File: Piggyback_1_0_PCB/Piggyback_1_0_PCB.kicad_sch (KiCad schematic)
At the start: 39 parts, among them J1 Conn_01x04_Female, J10 Conn_02x04_Odd_Even, J11 Conn_02x04_Odd_Even, J12 Conn_01x04_Female, J13 Conn_01x04_Female, J2 Conn_02x04_Odd_Even, J3 Conn_01x04_Female, J4 Conn_02x04_Odd_Even, J5 Conn_01x04_Female, J6 Conn_01x04_Female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

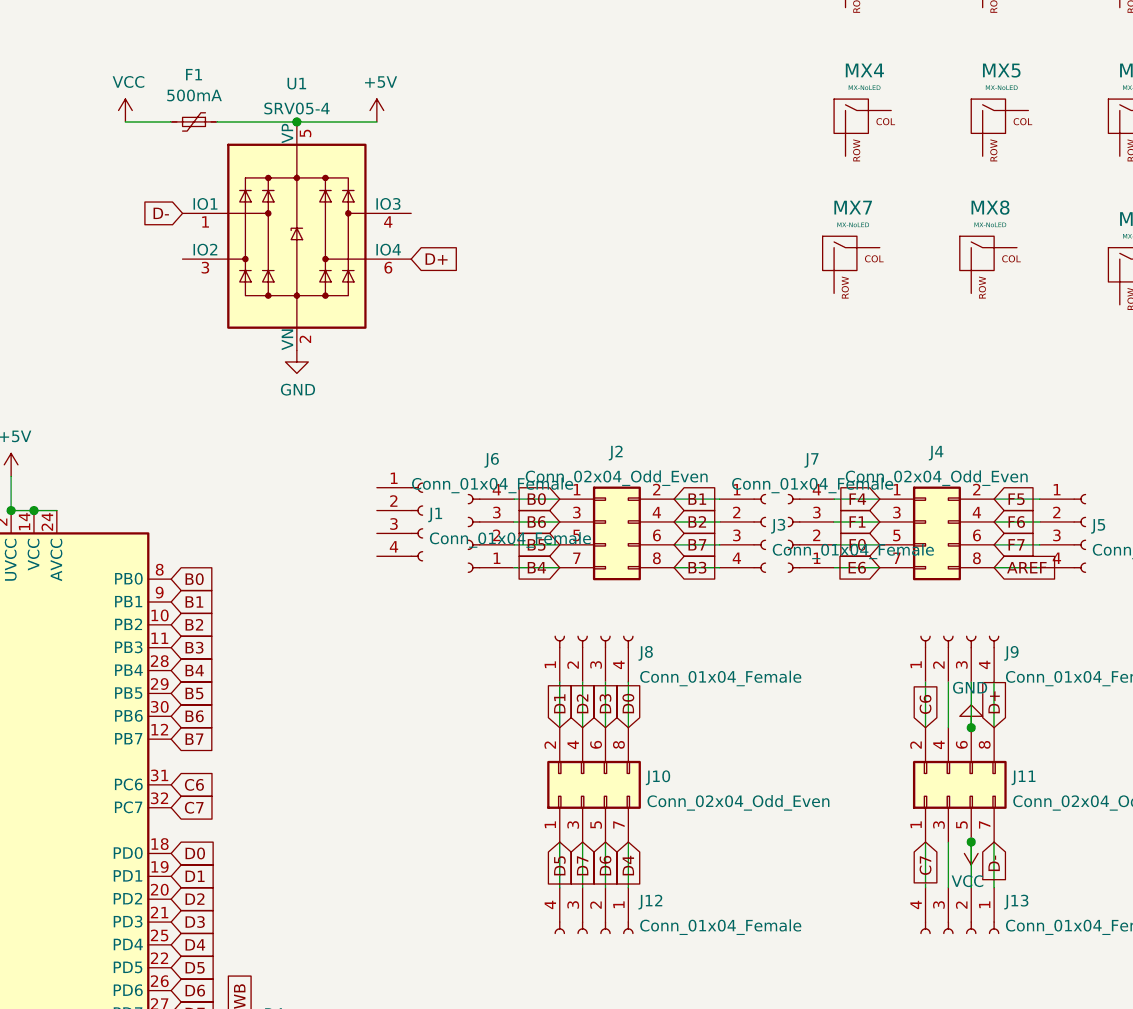
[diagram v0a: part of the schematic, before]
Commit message: Connected NC pads to GND and 5V
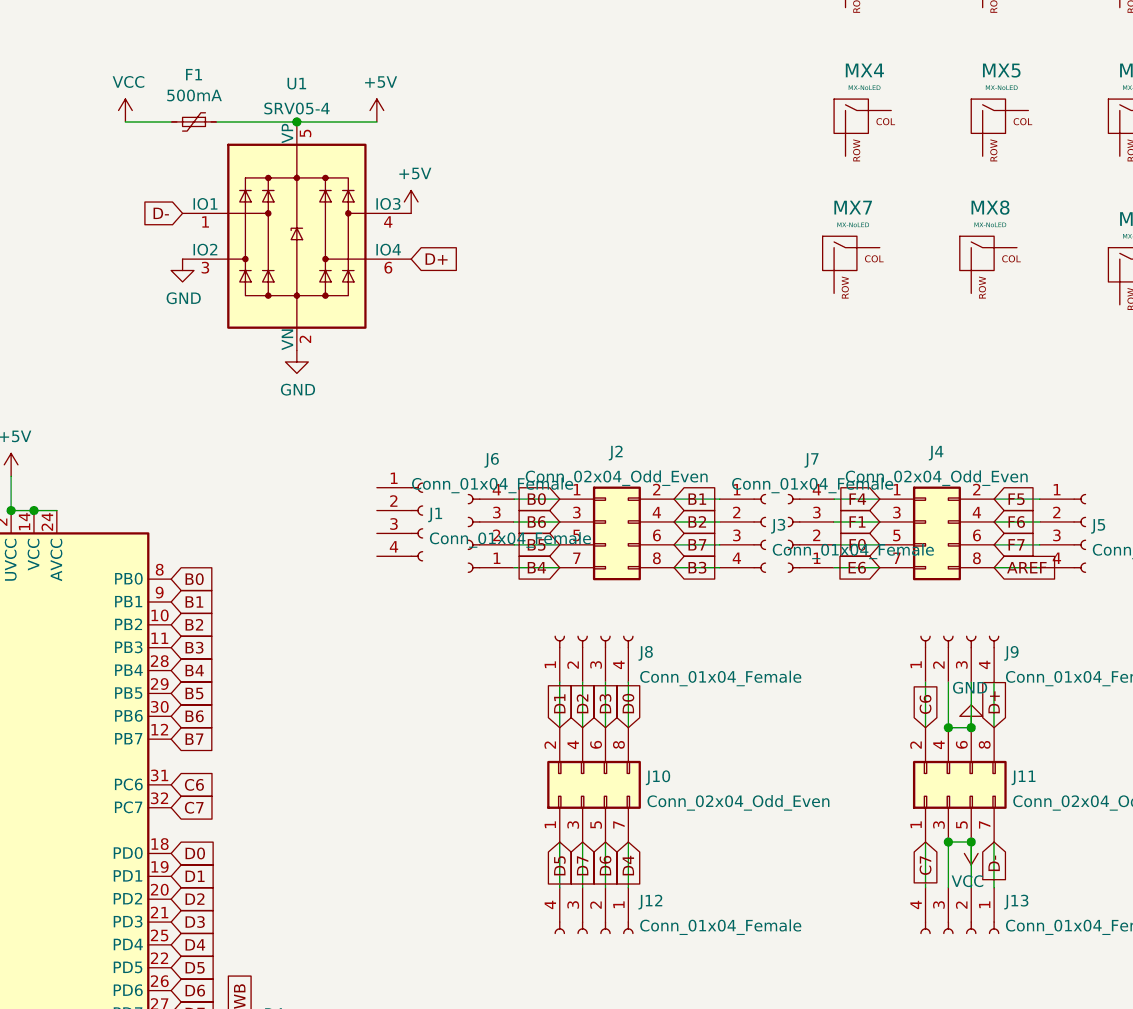
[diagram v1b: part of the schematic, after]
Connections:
- net +5V: now also U1.4 (IO3)
- net GND: now also J11.4 (Pin_4), J9.2 (Pin_2), U1.3 (IO2)
- net VCC: now also J11.3 (Pin_3), J13.3 (Pin_3)
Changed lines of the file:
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@@
   (junction (at 58.42 97.79) (diameter 1.016) (color 0 0 0 0))
   (junction (at 87.63 54.61) (diameter 1.016) (color 0 0 0 0))
+  (junction (at 160.02 121.92) (diameter 1.016) (color 0 0 0 0))
+  (junction (at 160.02 134.62) (diameter 1.016) (color 0 0 0 0))
   (junction (at 162.56 121.92) (diameter 1.016) (color 0 0 0 0))
   (junction (at 162.56 134.62) (diameter 1.016) (color 0 0 0 0))
@@
     (stroke (width 0) (type solid) (color 0 0 0 0))
   )
+  (wire (pts (xy 160.02 121.92) (xy 162.56 121.92))
+    (stroke (width 0) (type solid) (color 0 0 0 0))
+  )
+  (wire (pts (xy 160.02 134.62) (xy 162.56 134.62))
+    (stroke (width 0) (type solid) (color 0 0 0 0))
+  )
   (wire (pts (xy 160.02 139.7) (xy 160.02 134.62))
     (stroke (width 0) (type solid) (color 0 0 0 0))
@@
     (pin "1")
   )
+  (symbol (lib_id "power:+5V") (at 100.33 64.77 0) (unit 1)
+    (in_bom yes) (on_board yes)
+    (property "Reference" "#PWR?" (id 0) (at 100.33 68.58 0)
+      (effects (font (size 1.27 1.27)) hide)
+    )
+    (property "Value" "+5V" (id 1) (at 100.711 60.3758 0))
+    (property "Footprint" "" (id 2) (at 100.33 64.77 0)
+      (effects (font (size 1.27 1.27)) hide)
+    )
+    (property "Datasheet" "" (id 3) (at 100.33 64.77 0)
+      (effects (font (size 1.27 1.27)) hide)
+    )
+    (pin "1")
+  )
   (symbol (lib_id "power:VCC") (at 162.56 134.62 180) (unit 1)
     (in_bom yes) (on_board yes)
@@
     )
     (property "Datasheet" "" (id 3) (at 46.99 189.23 0)
+      (effects (font (size 1.27 1.27)) hide)
+    )
+    (pin "1")
+  )
+  (symbol (lib_id "power:GND") (at 74.93 69.85 0) (unit 1)
+    (in_bom yes) (on_board yes)
+    (property "Reference" "#PWR?" (id 0) (at 74.93 76.2 0)
+      (effects (font (size 1.27 1.27)) hide)
+    )
+    (property "Value" "GND" (id 1) (at 75.057 74.2442 0))
+    (property "Footprint" "" (id 2) (at 74.93 69.85 0)
+      (effects (font (size 1.27 1.27)) hide)
+    )
+    (property "Datasheet" "" (id 3) (at 74.93 69.85 0)
       (effects (font (size 1.27 1.27)) hide)
     )
@@
       (reference "#PWR015") (unit 1) (value "GND") (footprint "")
     )
+    (path "/17c3b27b-9240-45e7-959c-6ec7ce1baf30"
+      (reference "#PWR?") (unit 1) (value "GND") (footprint "")
+    )
+    (path "/ea83a73c-d8da-4553-a841-7ce78eb0de41"
+      (reference "#PWR?") (unit 1) (value "+5V") (footprint "")
+    )
     (path "/00000000-0000-0000-0000-000060f5800f"

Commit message: Changes for FAB
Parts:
- removed MX1, MX2, MX3, MX4, MX5, MX6, MX7, MX8, MX9: MX-NoLED, MX_Only:MXOnly-1U-NoLED, symbol MX_Alps_Hybrid:MX-NoLED
- Y1: footprint Crystal:Crystal_SMD_3225-4Pin_3.2x2.5mm -> Crystal:Crystal_SMD_2520-4Pin_2.5x2.0mm
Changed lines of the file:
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@@
   (symbol (lib_id "power:+5V") (at 100.33 64.77 0) (unit 1)
     (in_bom yes) (on_board yes)
-    (property "Reference" "#PWR?" (id 0) (at 100.33 68.58 0)
+    (property "Reference" "#PWR0102" (id 0) (at 100.33 68.58 0)
       (effects (font (size 1.27 1.27)) hide)
     )
@@
   (symbol (lib_id "power:GND") (at 74.93 69.85 0) (unit 1)
     (in_bom yes) (on_board yes)
-    (property "Reference" "#PWR?" (id 0) (at 74.93 76.2 0)
+    (property "Reference" "#PWR0101" (id 0) (at 74.93 76.2 0)
       (effects (font (size 1.27 1.27)) hide)
     )
@@
       (effects (font (size 1.27 1.27)) (justify left))
     )
-    (property "Footprint" "Crystal:Crystal_SMD_3225-4Pin_3.2x2.5mm" (id 2) (at 31.75 113.03 0)
+    (property "Footprint" "Crystal:Crystal_SMD_2520-4Pin_2.5x2.0mm" (id 2) (at 31.75 113.03 0)
       (effects (font (size 1.27 1.27)) hide)
     )
@@
     (property "Datasheet" "~" (id 3) (at 30.48 96.52 0)
       (effects (font (size 1.27 1.27)) hide)
-    )
-    (pin "1")
-    (pin "2")
-  )
-  (symbol (lib_id "MX_Alps_Hybrid:MX-NoLED") (at 148.59 69.85 0) (unit 1)
-    (in_bom yes) (on_board yes)
-    (property "Reference" "MX7" (id 0) (at 149.4282 64.1858 0)
-      (effects (font (size 1.524 1.524)))
-    )
-    (property "Value" "MX-NoLED" (id 1) (at 149.4282 66.0654 0)
-      (effects (font (size 0.508 0.508)))
-    )
-    (property "Footprint" "MX_Only:MXOnly-1U-NoLED" (id 2) (at 132.715 70.485 0)
-      (effects (font (size 1.524 1.524)) hide)
-    )
-    (property "Datasheet" "" (id 3) (at 132.715 70.485 0)
-      (effects (font (size 1.524 1.524)) hide)
-    )
-    (pin "1")
-    (pin "2")
-  )
-  (symbol (lib_id "MX_Alps_Hybrid:MX-NoLED") (at 149.86 38.1 0) (unit 1)
-    (in_bom yes) (on_board yes)
-    (property "Reference" "MX1" (id 0) (at 150.6982 32.4358 0)
-      (effects (font (size 1.524 1.524)))
-    )
-    (property "Value" "MX-NoLED" (id 1) (at 150.6982 34.3154 0)
-      (effects (font (size 0.508 0.508)))
-    )
-    (property "Footprint" "MX_Only:MXOnly-1U-NoLED" (id 2) (at 133.985 38.735 0)
-      (effects (font (size 1.524 1.524)) hide)
-    )
-    (property "Datasheet" "" (id 3) (at 133.985 38.735 0)
-      (effects (font (size 1.524 1.524)) hide)
-    )
-    (pin "1")
-    (pin "2")
-  )
-  (symbol (lib_id "MX_Alps_Hybrid:MX-NoLED") (at 149.86 54.61 0) (unit 1)
-    (in_bom yes) (on_board yes)
-    (property "Reference" "MX4" (id 0) (at 150.6982 48.9458 0)
-      (effects (font (size 1.524 1.524)))
-    )
-    (property "Value" "MX-NoLED" (id 1) (at 150.6982 50.8254 0)
-      (effects (font (size 0.508 0.508)))
-    )
-    (property "Footprint" "MX_Only:MXOnly-1U-NoLED" (id 2) (at 133.985 55.245 0)
-      (effects (font (size 1.524 1.524)) hide)
-    )
-    (property "Datasheet" "" (id 3) (at 133.985 55.245 0)
-      (effects (font (size 1.524 1.524)) hide)
-    )
-    (pin "1")
-    (pin "2")
-  )
-  (symbol (lib_id "MX_Alps_Hybrid:MX-NoLED") (at 163.83 69.85 0) (unit 1)
-    (in_bom yes) (on_board yes)
-    (property "Reference" "MX8" (id 0) (at 164.6682 64.1858 0)
-      (effects (font (size 1.524 1.524)))
-    )
-    (property "Value" "MX-NoLED" (id 1) (at 164.6682 66.0654 0)
-      (effects (font (size 0.508 0.508)))
-    )
-    (property "Footprint" "MX_Only:MXOnly-1U-NoLED" (id 2) (at 147.955 70.485 0)
-      (effects (font (size 1.524 1.524)) hide)
-    )
-    (property "Datasheet" "" (id 3) (at 147.955 70.485 0)
-      (effects (font (size 1.524 1.524)) hide)
-    )
-    (pin "1")
-    (pin "2")
-  )
-  (symbol (lib_id "MX_Alps_Hybrid:MX-NoLED") (at 165.1 38.1 0) (unit 1)
-    (in_bom yes) (on_board yes)
-    (property "Reference" "MX2" (id 0) (at 165.9382 32.4358 0)
-      (effects (font (size 1.524 1.524)))
-    )
-    (property "Value" "MX-NoLED" (id 1) (at 165.9382 34.3154 0)
-      (effects (font (size 0.508 0.508)))
-    )
-    (property "Footprint" "MX_Only:MXOnly-1U-NoLED" (id 2) (at 149.225 38.735 0)
-      (effects (font (size 1.524 1.524)) hide)
-    )
-    (property "Datasheet" "" (id 3) (at 149.225 38.735 0)
-      (effects (font (size 1.524 1.524)) hide)
-    )
-    (pin "1")
-    (pin "2")
-  )
-  (symbol (lib_id "MX_Alps_Hybrid:MX-NoLED") (at 165.1 54.61 0) (unit 1)
-    (in_bom yes) (on_board yes)
-    (property "Reference" "MX5" (id 0) (at 165.9382 48.9458 0)
-      (effects (font (size 1.524 1.524)))
-    )
-    (property "Value" "MX-NoLED" (id 1) (at 165.9382 50.8254 0)
-      (effects (font (size 0.508 0.508)))
-    )
-    (property "Footprint" "MX_Only:MXOnly-1U-NoLED" (id 2) (at 149.225 55.245 0)
-      (effects (font (size 1.524 1.524)) hide)
-    )
-    (property "Datasheet" "" (id 3) (at 149.225 55.245 0)
-      (effects (font (size 1.524 1.524)) hide)
-    )
-    (pin "1")
-    (pin "2")
-  )
-  (symbol (lib_id "MX_Alps_Hybrid:MX-NoLED") (at 180.34 38.1 0) (unit 1)
-    (in_bom yes) (on_board yes)
-    (property "Reference" "MX3" (id 0) (at 181.1782 32.4358 0)
-      (effects (font (size 1.524 1.524)))
-    )
-    (property "Value" "MX-NoLED" (id 1) (at 181.1782 34.3154 0)
-      (effects (font (size 0.508 0.508)))
-    )
-    (property "Footprint" "MX_Only:MXOnly-1U-NoLED" (id 2) (at 164.465 38.735 0)
-      (effects (font (size 1.524 1.524)) hide)
-    )
-    (property "Datasheet" "" (id 3) (at 164.465 38.735 0)
-      (effects (font (size 1.524 1.524)) hide)
-    )
-    (pin "1")
-    (pin "2")
-  )
-  (symbol (lib_id "MX_Alps_Hybrid:MX-NoLED") (at 180.34 54.61 0) (unit 1)
-    (in_bom yes) (on_board yes)
-    (property "Reference" "MX6" (id 0) (at 181.1782 48.9458 0)
-      (effects (font (size 1.524 1.524)))
-    )
-    (property "Value" "MX-NoLED" (id 1) (at 181.1782 50.8254 0)
-      (effects (font (size 0.508 0.508)))
-    )
-    (property "Footprint" "MX_Only:MXOnly-1U-NoLED" (id 2) (at 164.465 55.245 0)
-      (effects (font (size 1.524 1.524)) hide)
-    )
-    (property "Datasheet" "" (id 3) (at 164.465 55.245 0)
-      (effects (font (size 1.524 1.524)) hide)
-    )
-    (pin "1")
-    (pin "2")
-  )
-  (symbol (lib_id "MX_Alps_Hybrid:MX-NoLED") (at 180.34 71.12 0) (unit 1)
-    (in_bom yes) (on_board yes)
-    (property "Reference" "MX9" (id 0) (at 181.1782 65.4558 0)
-      (effects (font (size 1.524 1.524)))
-    )
-    (property "Value" "MX-NoLED" (id 1) (at 181.1782 67.3354 0)
-      (effects (font (size 0.508 0.508)))
-    )
-    (property "Footprint" "MX_Only:MXOnly-1U-NoLED" (id 2) (at 164.465 71.755 0)
-      (effects (font (size 1.524 1.524)) hide)
-    )
-    (property "Datasheet" "" (id 3) (at 164.465 71.755 0)
-      (effects (font (size 1.524 1.524)) hide)
     )
     (pin "1")
@@
     )
     (path "/17c3b27b-9240-45e7-959c-6ec7ce1baf30"
-      (reference "#PWR?") (unit 1) (value "GND") (footprint "")
+      (reference "#PWR0101") (unit 1) (value "GND") (footprint "")
     )
     (path "/ea83a73c-d8da-4553-a841-7ce78eb0de41"
-      (reference "#PWR?") (unit 1) (value "+5V") (footprint "")
+      (reference "#PWR0102") (unit 1) (value "+5V") (footprint "")
     )
     (path "/00000000-0000-0000-0000-000060f5800f"
@@
       (reference "J13") (unit 1) (value "Conn_01x04_Female") (footprint "Connector_PinHeader_2.54mm:PinHeader_1x04_P2.54mm_Vertical")
     )
-    (path "/00000000-0000-0000-0000-000060fb3622"
-      (reference "MX1") (unit 1) (value "MX-NoLED") (footprint "MX_Only:MXOnly-1U-NoLED")
-    )
-    (path "/00000000-0000-0000-0000-000060fbb882"
-      (reference "MX2") (unit 1) (value "MX-NoLED") (footprint "MX_Only:MXOnly-1U-NoLED")
-    )
-    (path "/00000000-0000-0000-0000-000060fc6043"
-      (reference "MX3") (unit 1) (value "MX-NoLED") (footprint "MX_Only:MXOnly-1U-NoLED")
-    )
-    (path "/00000000-0000-0000-0000-000060fbd2f8"
-      (reference "MX4") (unit 1) (value "MX-NoLED") (footprint "MX_Only:MXOnly-1U-NoLED")
-    )
-    (path "/00000000-0000-0000-0000-000060fbe8aa"
-      (reference "MX5") (unit 1) (value "MX-NoLED") (footprint "MX_Only:MXOnly-1U-NoLED")
-    )
-    (path "/00000000-0000-0000-0000-000060fc79cf"
-      (reference "MX6") (unit 1) (value "MX-NoLED") (footprint "MX_Only:MXOnly-1U-NoLED")
-    )
-    (path "/00000000-0000-0000-0000-000060fc9431"
-      (reference "MX7") (unit 1) (value "MX-NoLED") (footprint "MX_Only:MXOnly-1U-NoLED")
-    )
-    (path "/00000000-0000-0000-0000-000060fcac0d"
-      (reference "MX8") (unit 1) (value "MX-NoLED") (footprint "MX_Only:MXOnly-1U-NoLED")
-    )
-    (path "/00000000-0000-0000-0000-000060fcc8e8"
-      (reference "MX9") (unit 1) (value "MX-NoLED") (footprint "MX_Only:MXOnly-1U-NoLED")
-    )
     (path "/00000000-0000-0000-0000-000060f5ead5"
       (reference "R1") (unit 1) (value "10k") (footprint "Resistor_SMD:R_0402_1005Metric")
@@
     )
     (path "/00000000-0000-0000-0000-000060f55bc9"
-      (reference "Y1") (unit 1) (value "16MHz") (footprint "Crystal:Crystal_SMD_3225-4Pin_3.2x2.5mm")
-    )
-  )
+      (reference "Y1") (unit 1) (value "16MHz") (footprint "Crystal:Crystal_SMD_2520-4Pin_2.5x2.0mm")
+    )
+  )
